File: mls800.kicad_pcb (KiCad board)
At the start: 2 copper layers, 293.4 x 80.5 mm, 106 parts, among them CON1 BARREL_JACK, IC1 6N137, J1 USB, J10 NSJ8HC, J11 NRJ4HF-1, J2 NRJ4HF-1, J3 NSJ8HC, J4 NSJ8HC, J5 NSJ8HC, J6 NSJ8HC, J7 NSJ8HC, J8 NSJ8HC, J9 NSJ8HC, P1 CONN_02X03, P2 DIN_5, P3 DIN_5, P4 CONN_02X03, P5 CONN_02X03, SW10 SW_TACT_LED, SW11 SW_TACT_LED, SW12 SW_PUSH_RIGHT_ANGLE, SW2 SW_TACT_LED, SW3 SW_TACT_LED, SW4 SW_TACT_LED, SW5 SW_TACT_LED, SW6 SW_TACT_LED, SW7 SW_TACT_LED, SW8 SW_TACT_LED, SW9 SW_TACT_LED, U1 LM340MP-5.0/NOPB, U2 ATmega32U4-AU, U3 24LC256, U4 MCP23017, U5 AS1115, U6 ULN2803A, U7 ULN2803A, U8 LM340MP-5.0/NOPB, X1 16Mhz

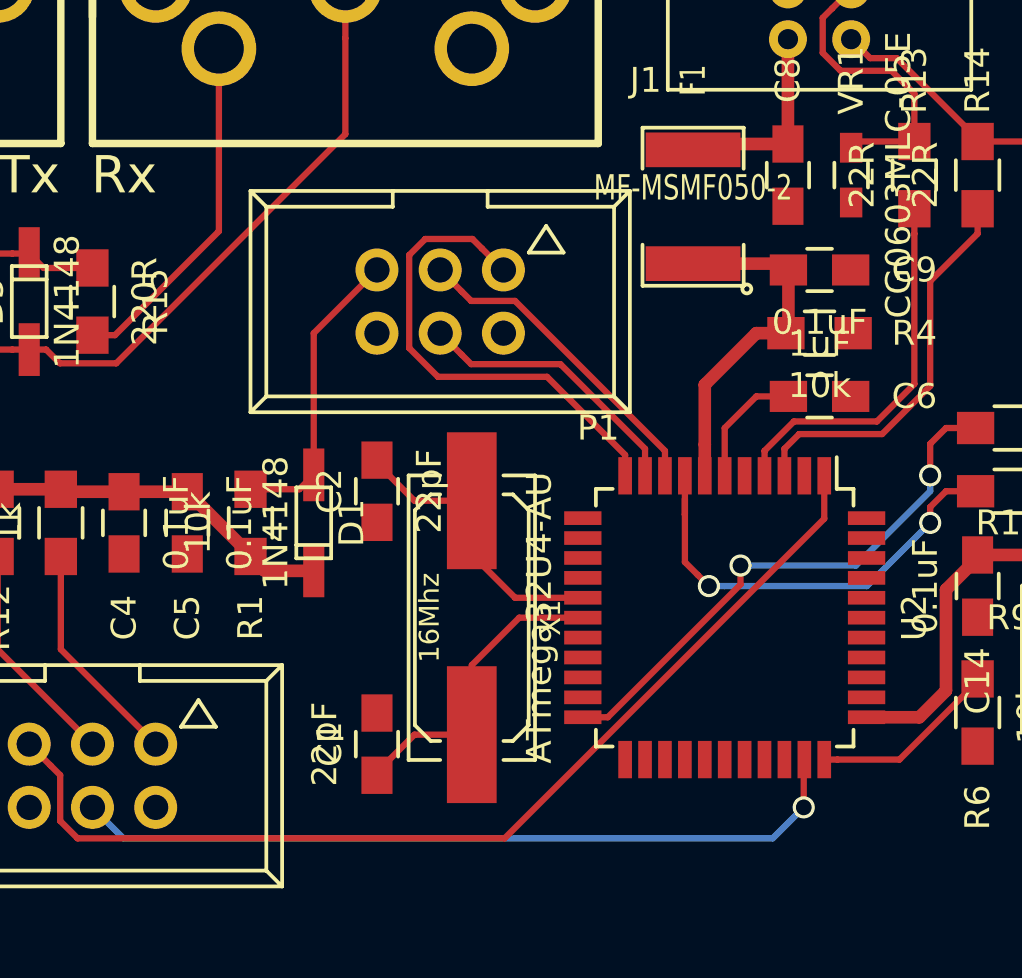
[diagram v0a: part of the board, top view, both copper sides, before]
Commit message: Optimized routing for copper plane
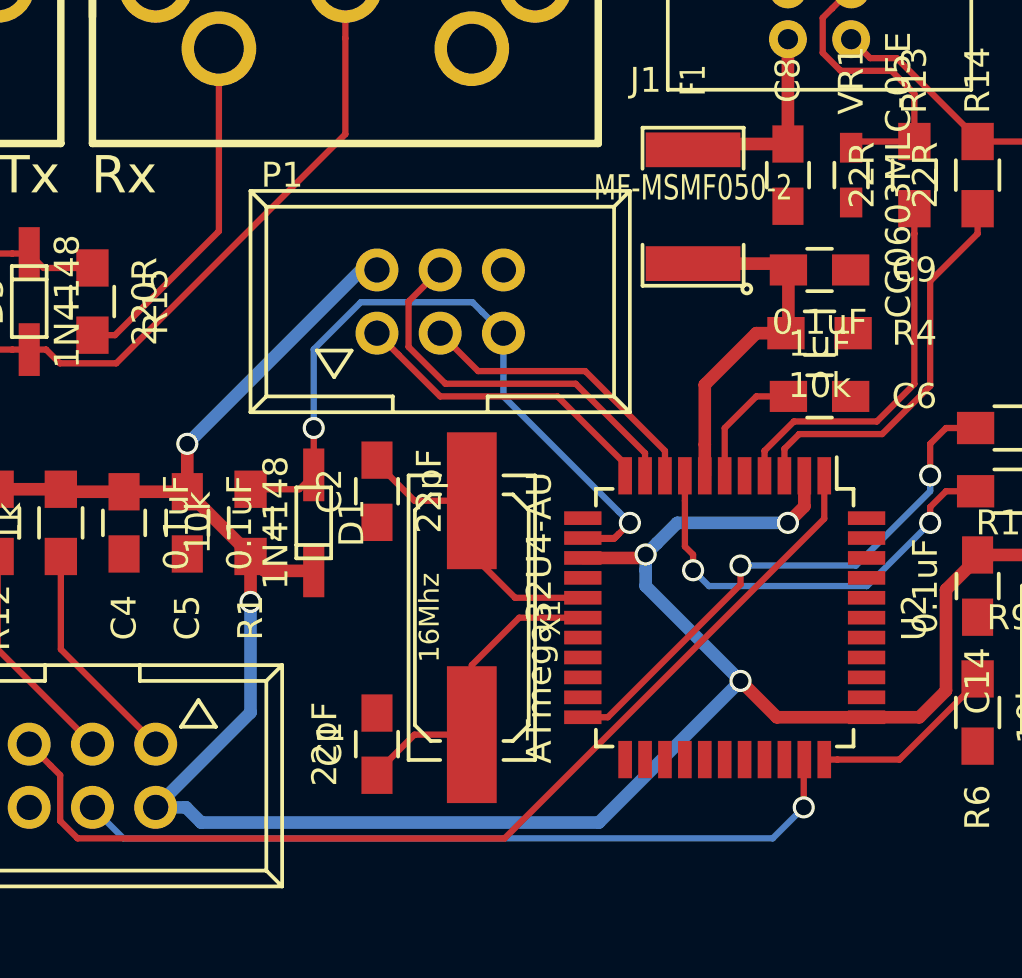
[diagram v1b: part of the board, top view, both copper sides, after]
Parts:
- turned P1 to 0 degrees
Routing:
- net VCC: track 96.5 -> 170.0 mm, vias 0 -> 5
- net /RESET: track 12.1 -> 30.1 mm, vias 0 -> 2
- net /MISO: track 19.6 -> 12.6 mm
- net /MOSI: track 11.2 -> 15.8 mm
- net Net-(RE4-Pad9): track 2.33 -> 5.39 mm
- net Net-(RE3-Pad9): track 15.8 -> 12.7 mm
- net /SCK: track 13.0 -> 12.0 mm
- net /RXLED: track 18.1 -> 17.5 mm

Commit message: Motherboard copper planes were off by a few centimeters Routing of data traces (sda, scl)
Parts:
- moved C12 1.80 mm to (244.5, 87.0)
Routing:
- net +5V: track 261.7 -> 363.8 mm, vias 17 -> 19
- net /RX: track 22.0 -> 63.3 mm, vias 1 -> 4
- net /Loops/SDA: track 14.3 -> 52.2 mm, vias 0 -> 1
- net /Loops/SCL: track 17.0 -> 54.1 mm, vias 0 -> 1
- net /RESET: track 30.1 -> 65.7 mm, vias 2 -> 3
- net Net-(RE4-Pad9): track 5.39 -> 2.33 mm
- net Net-(RE3-Pad9): track 12.7 -> 15.8 mm

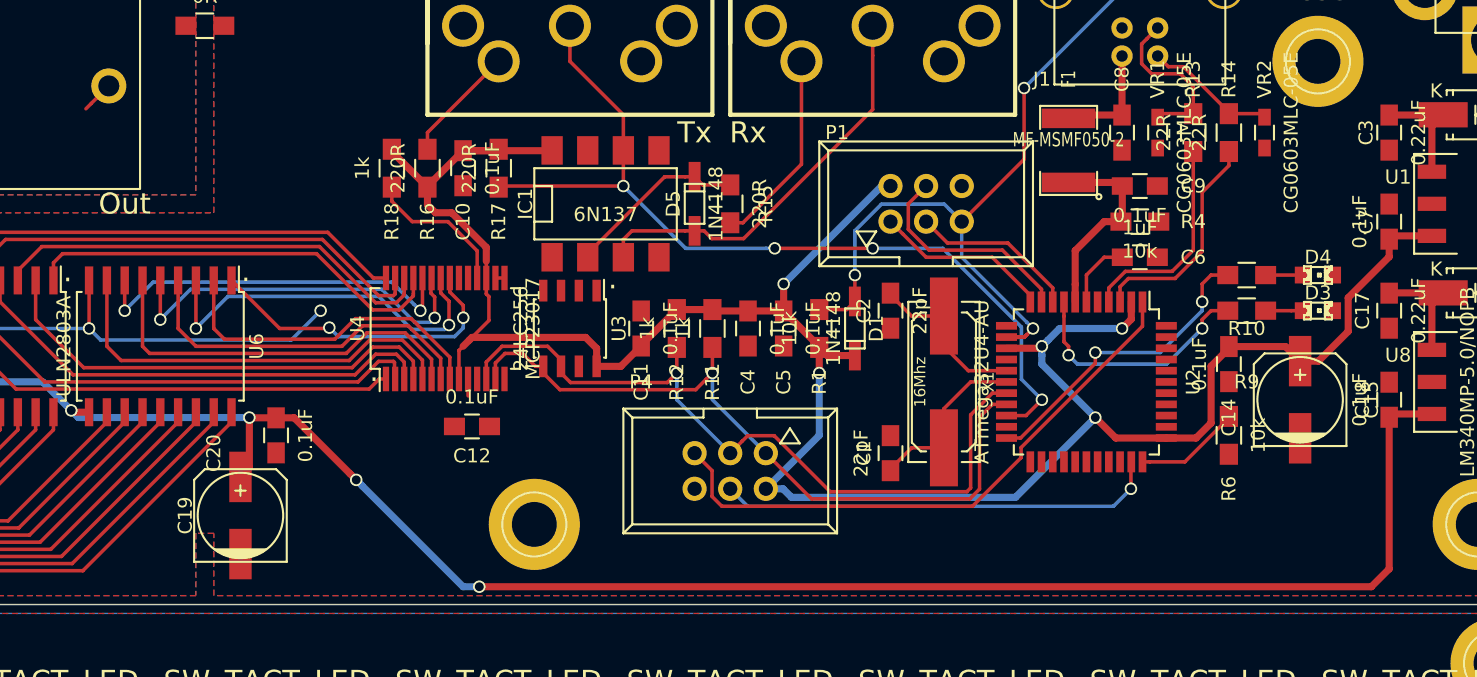
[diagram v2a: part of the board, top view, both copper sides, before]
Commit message: Done routing motherboard logic units
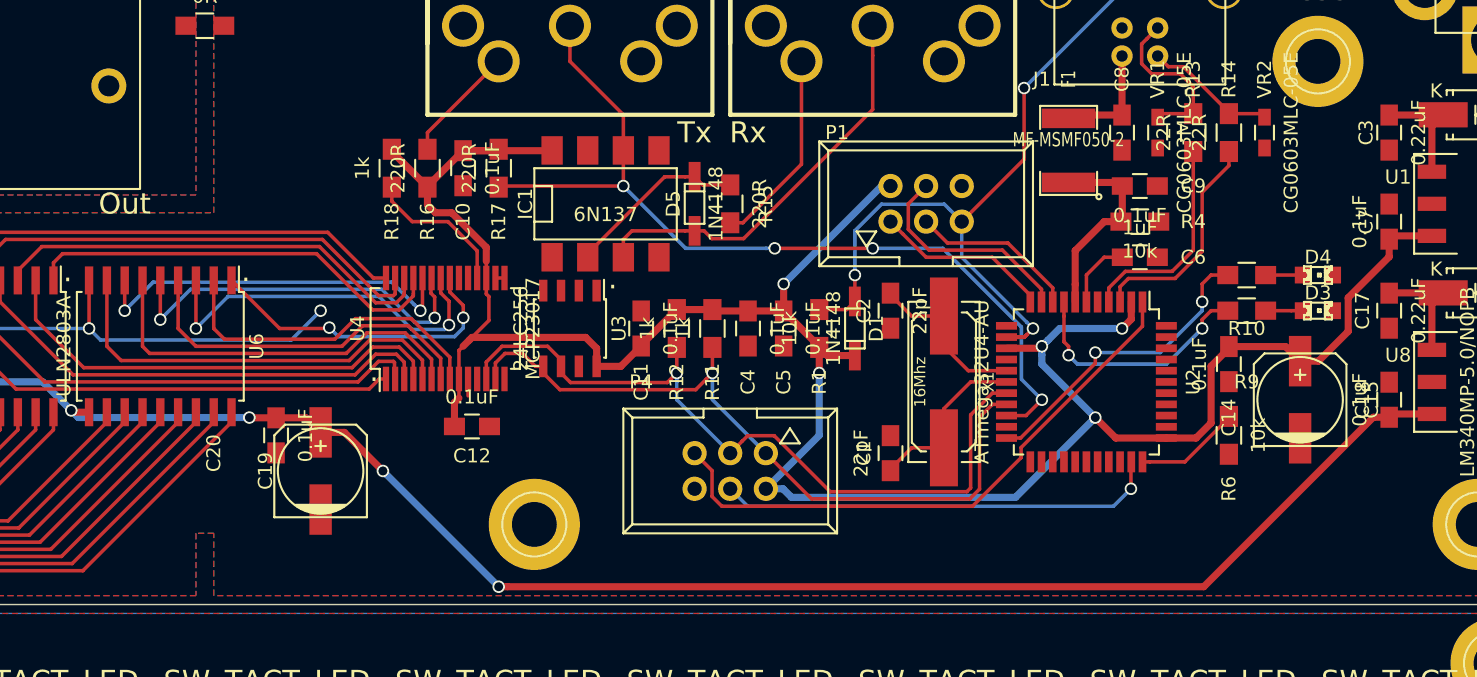
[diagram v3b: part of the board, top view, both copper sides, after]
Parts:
- moved C19 6.54 mm to (233.7, 90.2)
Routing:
- net +5V: track 363.8 -> 352.9 mm
- net VCC: track 169.8 -> 173.3 mm
- net Net-(J11-Pad1): track 2.31 -> 0.00 mm
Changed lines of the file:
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@@
   (general
     (links 345)
-    (no_connects 82)
-    (area 27.94 31.440001 350.9 142.1)
+    (no_connects 60)
+    (area 29.159999 45.161999 322.630001 125.780001)
     (thickness 1.6)
     (drawings 31)
@@
   )
   (module Capacitors_SMD:c_elec_6.3x7.7 (layer F.Cu)
-    (at 227.965 93.345 90)
+    (at 233.68 90.17 90)
     (descr "SMT capacitor, aluminium electrolytic, 6.3x7.7")
     (fp_text reference C19 (at 0 -3.937 90) (layer F.SilkS)
@@
   (segment (start 273.685 69.85) (end 274.32 69.85) (width 0.508) (layer B.Cu) (net 17))
   (segment (start 266.7 76.835) (end 273.685 69.85) (width 0.508) (layer B.Cu) (net 17))
+  (segment (start 243.225 85.294402) (end 243.545 84.974402) (width 0.508) (layer F.Cu) (net 17))
+  (segment (start 243.225 86.995) (end 243.225 85.294402) (width 0.508) (layer F.Cu) (net 17))
+  (segment (start 243.545 84.878434) (end 243.545 84.974402) (width 0.254) (layer F.Cu) (net 17))
+  (segment (start 243.545 83.61) (end 243.545 84.878434) (width 0.254) (layer F.Cu) (net 17))
   (segment (start 288.29 76.2) (end 288.29 78.12) (width 0.254) (layer F.Cu) (net 18))
   (segment (start 289.56 74.93) (end 288.29 76.2) (width 0.254) (layer F.Cu) (net 18))
@@
   (segment (start 77.86 64.332) (end 79.13 63.062) (width 0.254) (layer F.Cu) (net 34))
   (segment (start 82.55 84.035) (end 82.55 82.58) (width 0.254) (layer F.Cu) (net 35))
-  (segment (start 217.326001 63.961999) (end 218.576 62.712) (width 0.254) (layer F.Cu) (net 37))
-  (segment (start 216.944999 64.343001) (end 217.326001 63.961999) (width 0.254) (layer F.Cu) (net 37))
   (segment (start 284.29 78.12) (end 284.29 77.645) (width 0.254) (layer F.Cu) (net 38))
   (segment (start 284.29 77.645) (end 281.575 74.93) (width 0.254) (layer F.Cu) (net 38))
@@
   (segment (start 309.9 77.47) (end 309.88 77.49) (width 0.508) (layer F.Cu) (net 116))
   (segment (start 313.73064 77.47) (end 309.9 77.47) (width 0.508) (layer F.Cu) (net 116))
+  (segment (start 247.008617 98.425) (end 246.38 98.425) (width 0.508) (layer F.Cu) (net 117))
+  (segment (start 296.662 98.425) (end 247.008617 98.425) (width 0.508) (layer F.Cu) (net 117))
+  (segment (start 308.747 86.34) (end 296.662 98.425) (width 0.508) (layer F.Cu) (net 117))
+  (segment (start 309.88 86.34) (end 308.747 86.34) (width 0.508) (layer F.Cu) (net 117))
+  (segment (start 238.125 90.17) (end 246.38 98.425) (width 0.508) (layer B.Cu) (net 117))
+  (via (at 246.38 98.425) (size 0.889) (drill 0.635) (layers F.Cu B.Cu) (net 117))
+  (segment (start 233.68 87.41918) (end 235.37418 87.41918) (width 0.508) (layer F.Cu) (net 117))
+  (segment (start 235.37418 87.41918) (end 238.125 90.17) (width 0.508) (layer F.Cu) (net 117))
+  (via (at 238.125 90.17) (size 0.889) (drill 0.635) (layers F.Cu B.Cu) (net 117))
+  (segment (start 230.505 86.38) (end 232.64082 86.38) (width 0.508) (layer F.Cu) (net 117))
+  (segment (start 232.64082 86.38) (end 233.68 87.41918) (width 0.508) (layer F.Cu) (net 117))
   (segment (start 199.39 84.035) (end 198.432 84.035) (width 0.508) (layer F.Cu) (net 117))
   (segment (start 198.432 84.035) (end 193.567 88.9) (width 0.508) (layer F.Cu) (net 117))
@@
   (segment (start 228.6 86.36) (end 216.408 86.36) (width 0.508) (layer B.Cu) (net 117))
   (via (at 228.6 86.36) (size 0.889) (drill 0.635) (layers F.Cu B.Cu) (net 117))
-  (segment (start 228.6 89.95918) (end 228.6 86.36) (width 0.508) (layer F.Cu) (net 117))
-  (segment (start 227.965 90.59418) (end 228.6 89.95918) (width 0.508) (layer F.Cu) (net 117))
   (segment (start 228.62 86.38) (end 228.6 86.36) (width 0.508) (layer F.Cu) (net 117))
   (segment (start 230.505 86.38) (end 228.62 86.38) (width 0.508) (layer F.Cu) (net 117))
-  (segment (start 309.88 97.155) (end 309.88 86.34) (width 0.508) (layer F.Cu) (net 117))
-  (segment (start 308.61 98.425) (end 309.88 97.155) (width 0.508) (layer F.Cu) (net 117))
-  (via (at 244.995686 98.425) (size 0.889) (drill 0.635) (layers F.Cu B.Cu) (net 117))
-  (segment (start 244.995686 98.425) (end 308.61 98.425) (width 0.508) (layer F.Cu) (net 117))
-  (via (at 236.22 90.805) (size 0.889) (drill 0.635) (layers F.Cu B.Cu) (net 117))
-  (segment (start 244.995686 98.425) (end 243.84 98.425) (width 0.508) (layer B.Cu) (net 117))
-  (segment (start 243.84 98.425) (end 236.664499 91.249499) (width 0.508) (layer B.Cu) (net 117))
-  (segment (start 236.664499 91.249499) (end 236.22 90.805) (width 0.508) (layer B.Cu) (net 117))
-  (segment (start 230.505 86.38) (end 231.795 86.38) (width 0.508) (layer F.Cu) (net 117))
-  (segment (start 231.795 86.38) (end 235.775501 90.360501) (width 0.508) (layer F.Cu) (net 117))
-  (segment (start 235.775501 90.360501) (end 236.22 90.805) (width 0.508) (layer F.Cu) (net 117))
-  (segment (start 118.11 78.144) (end 116.84 79.414) (width 0.254) (layer F.Cu) (net 120))
   (segment (start 118.11 75.985) (end 118.11 78.144) (width 0.254) (layer F.Cu) (net 120))
+  (segment (start 118.11 78.144) (end 116.84 79.414) (width 0.254) (layer F.Cu) (net 120))
   (segment (start 116.84 86.36) (end 118.11 87.63) (width 0.254) (layer F.Cu) (net 120))
   (segment (start 116.84 79.414) (end 116.84 86.36) (width 0.254) (layer F.Cu) (net 120))
